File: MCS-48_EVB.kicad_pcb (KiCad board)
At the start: 2 copper layers, 37 parts, among them CON1 BARREL_JACK, P1 CONN_01X06, P10 CONN_01X08, P11 CONN_01X06, P2 CONN_01X06, P3 CONN_01X08, P4 CONN_01X08, P5 CONN_01X03, P6 CONN_01X03, P7 CONN_01X02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

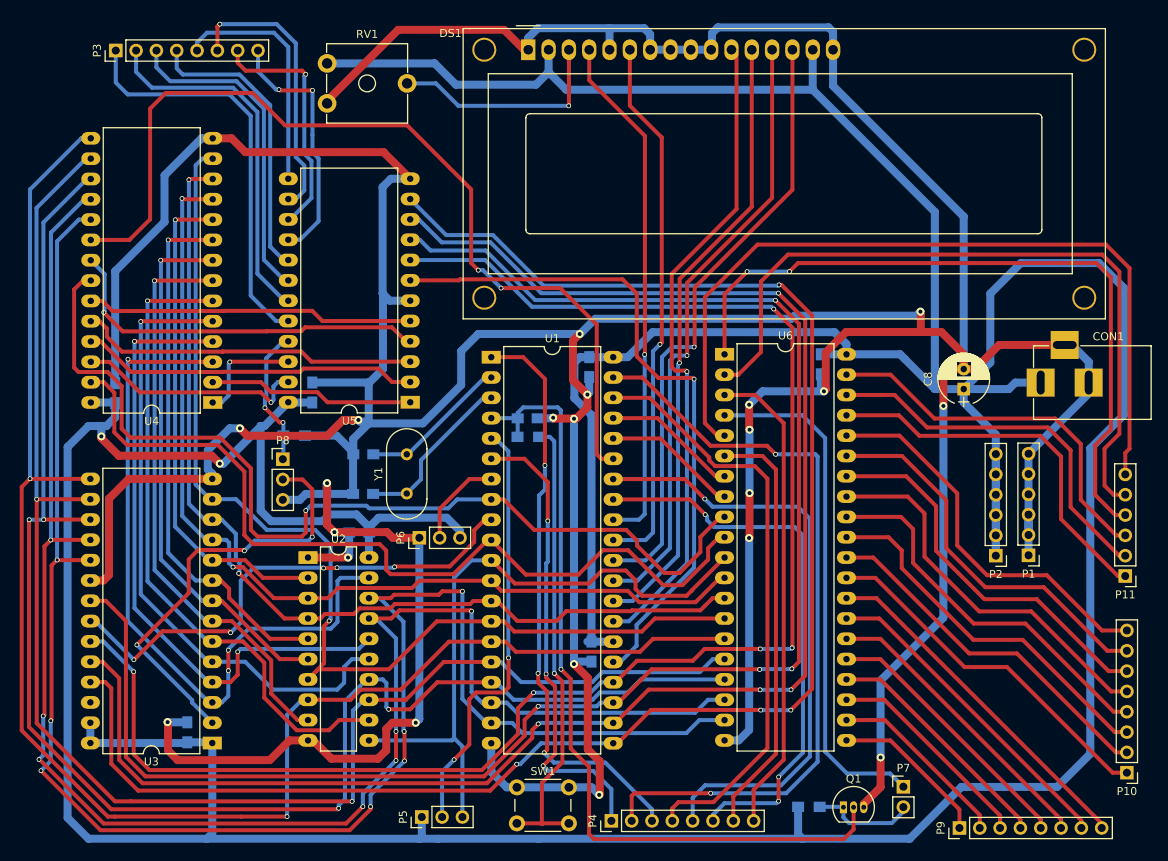
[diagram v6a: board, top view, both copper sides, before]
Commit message: Added GND planes
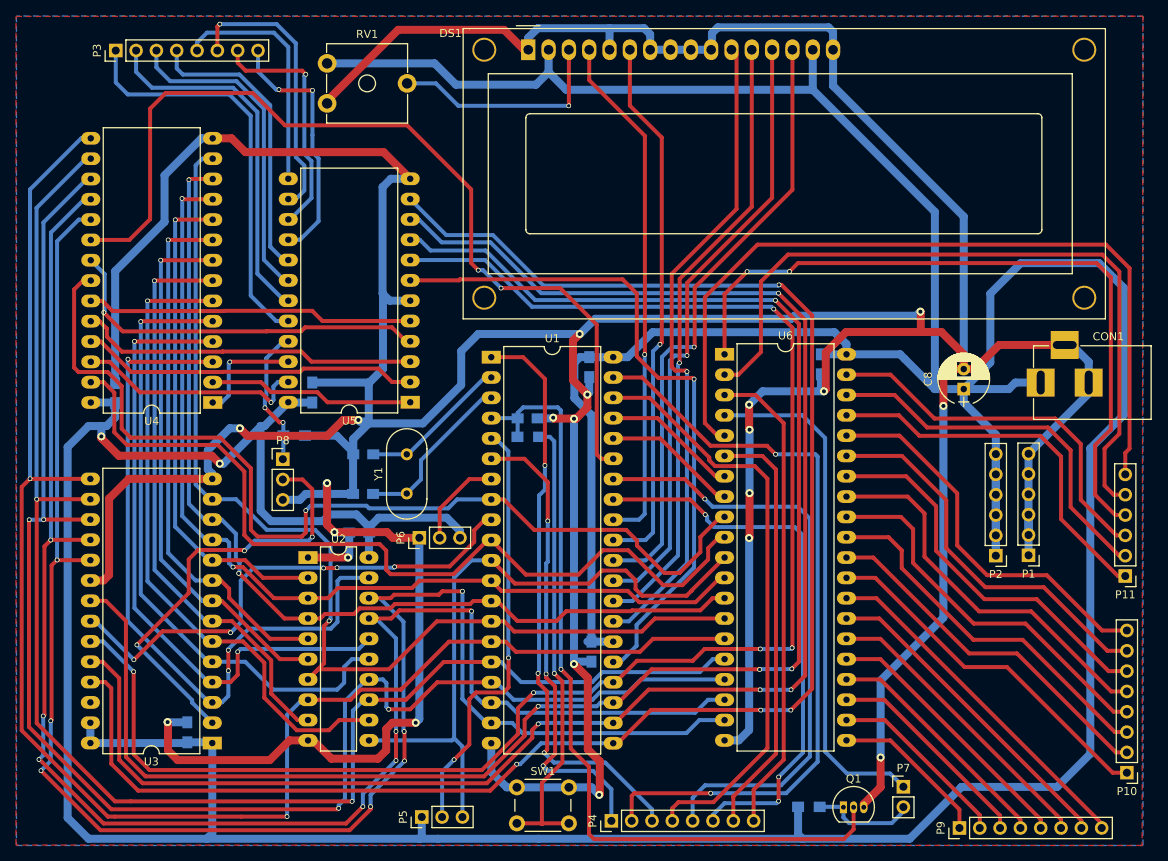
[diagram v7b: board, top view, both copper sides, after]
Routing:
- added copper zone on B.Cu, net GND
- added copper zone on F.Cu, net GND
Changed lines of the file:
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@@
     (last_trace_width 0.25)
     (trace_clearance 0.2)
-    (zone_clearance 0.508)
+    (zone_clearance 0.5)
     (zone_45_only no)
     (trace_min 0.2)
@@
   (segment (start 158.5204 89.9912) (end 160.6352 92.106) (width 1) (layer B.Cu) (net 1))
   (segment (start 160.6352 92.106) (end 160.6352 94.6912) (width 1) (layer B.Cu) (net 1))
-  (segment (start 149.0218 103.632) (end 149.0218 106.172) (width 1) (layer B.Cu) (net 2) (status C00000))
+  (segment (start 149.0218 103.632) (end 149.0218 106.172) (width 1) (layer B.Cu) (net 2))
   (segment (start 98.4758 127.0708) (end 98.4758 98.7552) (width 1) (layer B.Cu) (net 2))
   (segment (start 97.0334 91.5108) (end 98.1964 91.5108) (width 1) (layer B.Cu) (net 2))
@@
   (segment (start 42.037 95.9104) (end 57.15 95.9104) (width 0.5) (layer F.Cu) (net 93))
   (segment (start 38.227 92.1004) (end 42.037 95.9104) (width 0.5) (layer F.Cu) (net 93))
+  (zone (net 1) (net_name GND) (layer F.Cu) (hatch edge 0.508)
+    (connect_pads (clearance 0.5))
+    (min_thickness 0.2)
+    (fill yes (arc_segments 16) (thermal_gap 0.508) (thermal_bridge_width 0.508))
+    (polygon
+      (pts
+        (xy 167.3098 152.5524) (xy 26.543 152.5016) (xy 26.543 48.9204) (xy 167.4114 48.895)
+      )
+    )
+  )
+  (zone (net 1) (net_name GND) (layer B.Cu) (hatch edge 0.508)
+    (connect_pads (clearance 0.5))
+    (min_thickness 0.2)
+    (fill yes (arc_segments 16) (thermal_gap 0.508) (thermal_bridge_width 0.508))
+    (polygon
+      (pts
+        (xy 26.5938 48.895) (xy 26.5938 152.5524) (xy 167.4114 152.5524) (xy 167.4114 48.895) (xy 26.5938 48.8696)
+      )
+    )
+  )
 )
